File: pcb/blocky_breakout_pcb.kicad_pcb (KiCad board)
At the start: 4 copper layers, 85 x 61 mm, 94 parts, among them J1 Raspberry_Pi_4, J10 Conn_01x02_Pin, J11 Conn_01x02_Pin, J12 Conn_01x02_Pin, J2 USB_C_Receptacle_USB2.0_16P, J3 Conn_01x14_Pin, J4 Conn_01x08_Pin, J5 Conn_01x10_Pin, J6 Conn_01x06_Pin, J7 Conn_01x08_Pin, J9 Conn_01x03_Pin, K1 EE2-3TNUH, K2 EE2-3TNUH, Q1 DMG1012TQ-7, Q2 DMG1012TQ-7, SW1 SW_Push, SW2 SW_DIP_x04, SW3 SW_Push, U1 W25Q32JVSS, U2 NUP2202, U3 RP2350, U4 LM4040C33FTA, U5 LM66100DCK, U6 AOZ1280CI, U7 LM66100DCK, U8 MCP4728, U9 TCR2EE11, Y1 12Mhz

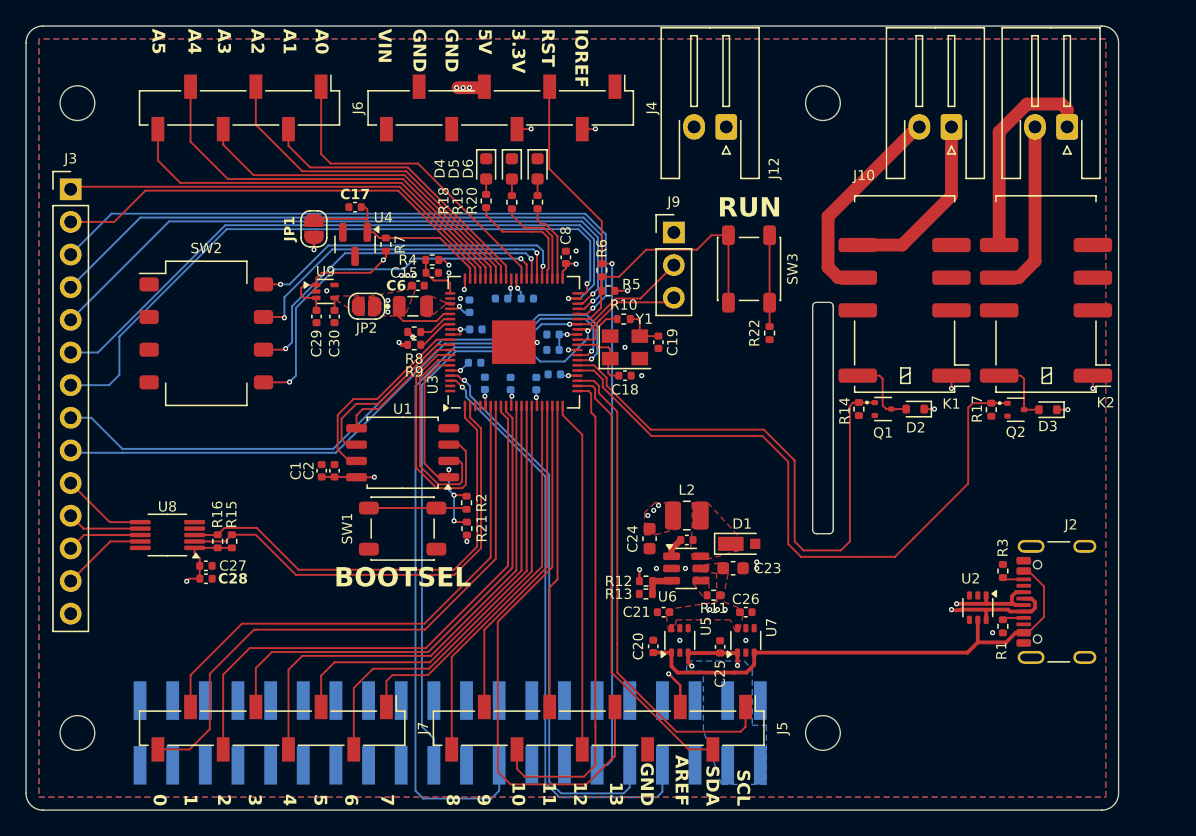
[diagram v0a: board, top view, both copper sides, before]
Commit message: Added gerbers, added 2x3 Arduino header.
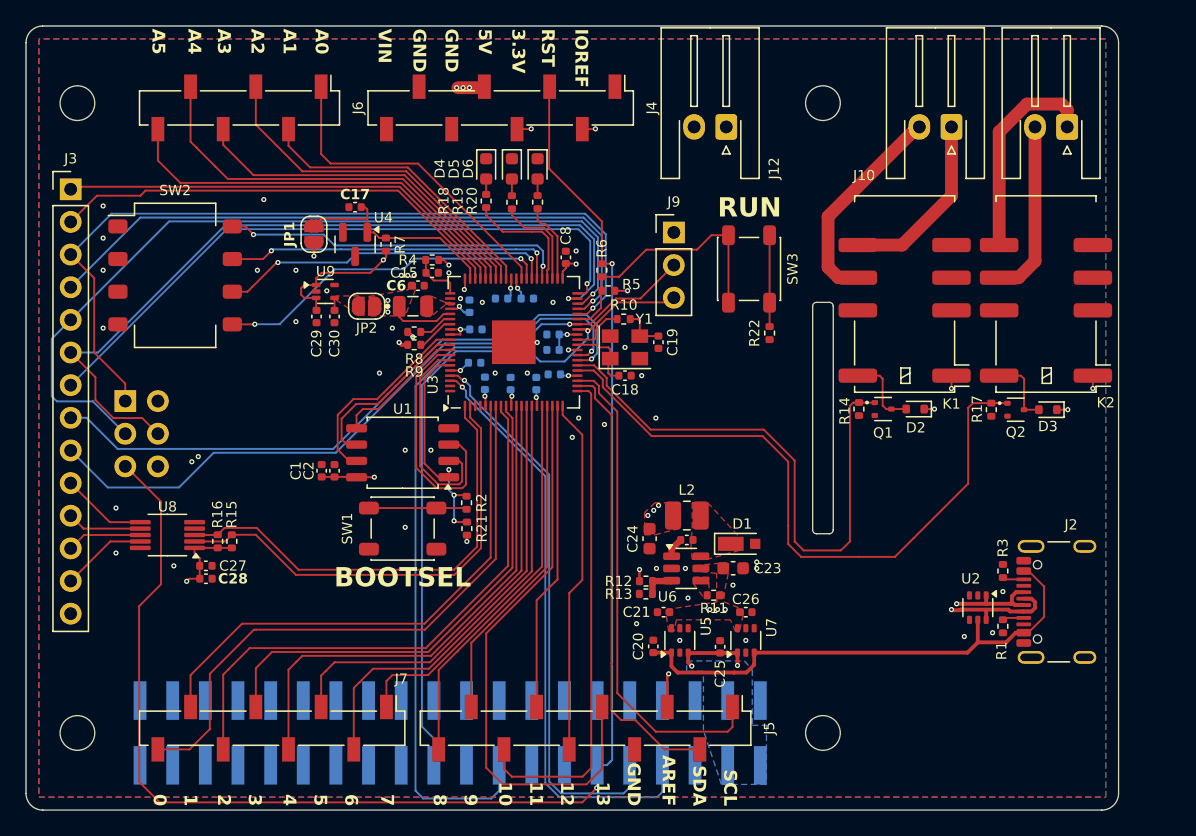
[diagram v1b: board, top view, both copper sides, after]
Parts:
- added J8: Conn_02x03_Odd_Even, Connector_PinSocket_2.54mm:PinSocket_2x03_P2.54mm_Vertical, B.Cu at (108.7, 95.2)
- moved SW2 5.12 mm to (112.6, 85.4)
- moved J5 1.02 mm to (144.5, 120.6)
- moved JP1 0.42 mm to (123.4, 82.2)
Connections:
- net /RP2350/GPIO28 renamed /Arduino Headers/SPI1.MISO
- net /RP2350/GPIO29 renamed /Arduino Headers/SPI1.CS
- net /RP2350/GPIO30 renamed /Arduino Headers/SPI1.SCK
- net /RP2350/GPIO31 renamed /Arduino Headers/SPI1.MOSI
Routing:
- net /Arduino Headers/RST: track 56.5 -> 121.4 mm, vias 1 -> 2
- net /Arduino Headers/SPI1.SCK: track 50.8 -> 64.3 mm
- net /Arduino Headers/SPI1.MISO: track 51.2 -> 64.3 mm
- net /Arduino Headers/SPI1.MOSI: track 51.9 -> 62.4 mm
- net /RP2350/GPIO39: track 28.8 -> 26.3 mm
- net /RP2350/GPIO27: track 48.5 -> 50.7 mm
- net /RP2350/GPIO36: track 25.3 -> 27.1 mm
- net /RP2350/GPIO32: track 52.4 -> 50.7 mm
- net /RP2350/GPIO38: track 27.3 -> 26.2 mm
- net /Arduino Headers/AREF: track 48.4 -> 47.6 mm
- net /Arduino Headers/I2C1.SDA: track 34.4 -> 35.2 mm
- net GND: vias 17 -> 48

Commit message: Added remaining part numbers, removed silk for holes, minor touchups
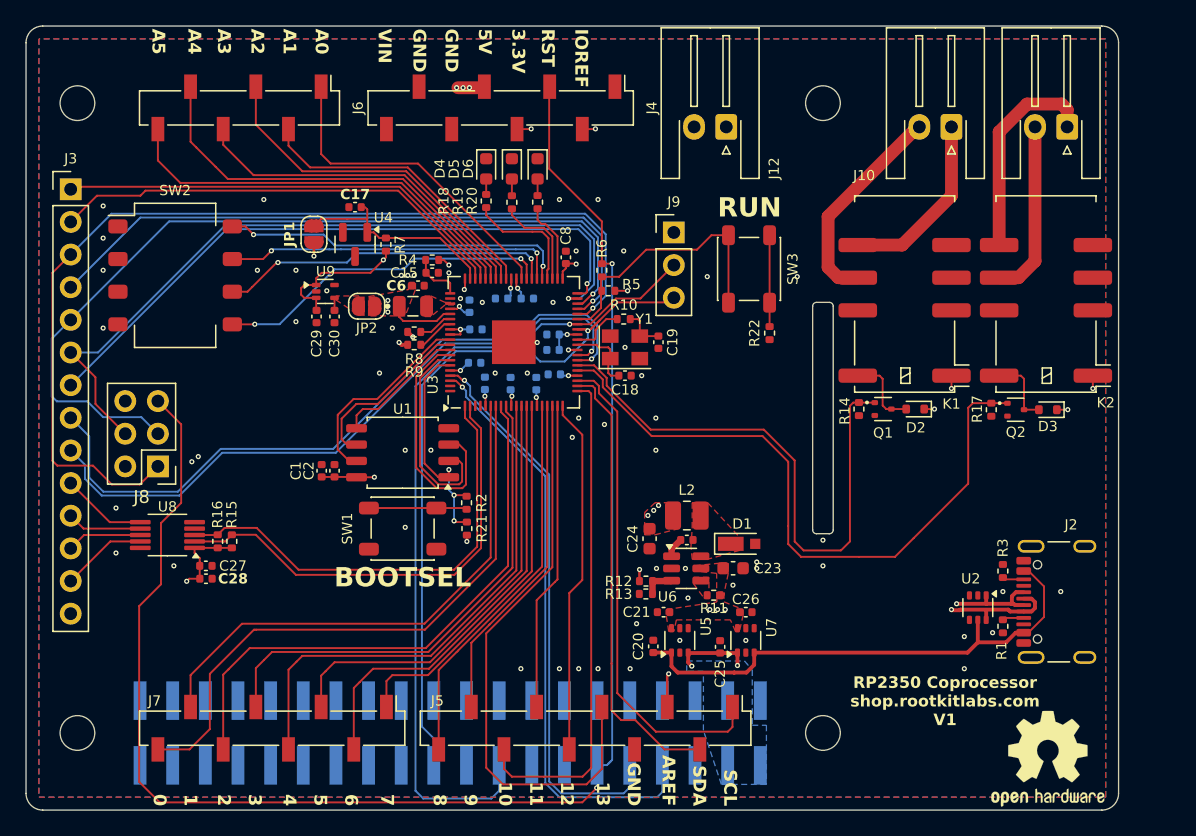
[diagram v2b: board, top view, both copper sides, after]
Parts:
- added REF**: OSHW-Logo2_9.8x8mm_SilkScreen, Symbol:OSHW-Logo2_9.8x8mm_SilkScreen, F.Cu at (180.5, 123.0)
- J8: footprint Connector_PinSocket_2.54mm:PinSocket_2x03_P2.54mm_Vertical -> Connector_PinHeader_2.54mm:PinHeader_2x03_P2.54mm_Vertical; moved to F.Cu
- moved J8 5.68 mm to (111.3, 100.3)
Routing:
- net /Arduino Headers/SPI1.MISO: track 64.3 -> 77.4 mm
- net /Arduino Headers/RST: track 121.4 -> 126.7 mm
- net /RP2350/GPIO26: track 50.6 -> 55.2 mm
- net /Arduino Headers/SPI1.SCK: track 64.3 -> 66.8 mm
- net /Arduino Headers/SPI1.MOSI: track 62.4 -> 60.0 mm
- net /RP2350/GPIO27: track 50.7 -> 51.9 mm
- net GND: vias 48 -> 63
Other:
- board text added: "RP2350 Coprocessor shop.rootkitlabs.com V1"

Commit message: R0.1 released
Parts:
- removed J12: Conn_01x02_Pin, Connector_JST:JST_XH_S2B-XH-A-1_1x02_P2.50mm_Horizontal
- D5: renamed from D2; value 1N4148WT -> BAT54XV2T1G
- D6: renamed from D3; value 1N4148WT -> BAT54XV2T1G
- J10, J11: value Conn_01x02_Pin -> Conn_01x03_Pin; footprint Connector_JST:JST_XH_S2B-XH-A-1_1x02_P2.50mm_Horizontal -> Connector_JST:JST_XH_S3B-XH-A-1_1x03_P2.50mm_Horizontal
- moved J1 4.00 mm to (186.3, 110.8)
- moved R2 4.00 mm to (181.0, 112.7)
- moved R4 4.00 mm to (181.0, 108.4)
- moved U2 4.00 mm to (179.1, 111.2)
- moved REF** 3.64 mm to (184.0, 122.0)
- moved J11 3.00 mm to (185.0, 73.9)
- moved D5 2.00 mm to (172.2, 95.8)
- moved D6 2.00 mm to (182.5, 95.8)
- moved K1 2.00 mm to (171.4, 86.8)
- moved K2 2.00 mm to (182.4, 86.8)
- moved Q1 2.00 mm to (169.7, 95.8)
- moved Q2 2.00 mm to (180.0, 95.8)
- moved R21 2.00 mm to (167.8, 95.8)
- moved R22 2.00 mm to (178.1, 95.8)
- moved J10 1.00 mm to (174.0, 73.9)
- renumbered C6 to C16, C25 to C22, C26 to C23, C22 to C24, C23 to C25, C24 to C26, C29 to C27, C30 to C28, C27 to C29, C28 to C30, C16 to C6, D4 to D1, D5 to D2, D6 to D3, D1 to D4, J2 to J1, J3 to J2, J9 to J3, J1 to J4, J4 to J5, J5 to J6, J6 to J7, J7 to J8, J8 to J9, R21 to R1, R8 to R10, R9 to R11, R10 to R12, R18 to R13, R19 to R14, R20 to R15, R11 to R16, R12 to R17, R13 to R18, R15 to R19, R1 to R2, R16 to R20, R14 to R21, R17 to R22, R2 to R3, R3 to R4, R4 to R5, R5 to R6, R6 to R7, R22 to R8, R7 to R9, SW3 to SW2, SW2 to SW3, U7 to U6, U6 to U7, U9 to U8, U8 to U9
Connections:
- K1 pad 10: unconnected-(K1-Pad10) -> Net-(J10-Pin_1)
- K1 pad 8: Net-(J10-Pin_1) -> Net-(J10-Pin_3)
- K2 pad 10: unconnected-(K2-Pad10) -> Net-(J11-Pin_1)
- K2 pad 8: Net-(J11-Pin_1) -> Net-(J11-Pin_3)
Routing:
- net Net-(J11-Pin_3): track 0.00 -> 9.66 mm
- net Net-(J10-Pin_3): track 0.00 -> 9.66 mm
- net Net-(J10-Pin_1): track 14.4 -> 18.4 mm
- net /RP2350/USB_D+: track 68.5 -> 72.5 mm
- net V_USB: track 40.2 -> 44.2 mm
- net /RP2350/USB_D-: track 67.8 -> 71.7 mm
- net Net-(J10-Pin_2): track 16.6 -> 14.3 mm
- net Net-(J11-Pin_1): track 16.4 -> 17.9 mm
- net Net-(J11-Pin_2): track 13.9 -> 14.5 mm
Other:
- board size 85 x 61 mm -> 89 x 61 mm
